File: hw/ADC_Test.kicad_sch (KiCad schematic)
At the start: 63 parts, among them J1 SMA in (perfboard), J2 9V IN, J3 PMOD (ZedBoard), U1 OPA2365, U2 OPA2365, U3 THS4531, U4 ADS7057, U5 AMS1117-3.3, U6 LM393, U7 AMS1117-5.0

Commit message: Add MON output, nWAKE DNP cap, ceramic-stable AVDD LDO, M3 holes
- J4 SMA MON: LPF_OUT through 51R (Basic C23197)
- C31 0603 DNP on nWAKE near J3
- AVDD: XC6206P332 (Basic, ceramic-stable) replaces AMS1117-3.3
- 5 V AMS1117: 22 uF tantalum output per datasheet
- H1/H2 M3 holes, CH silkscreen field, PMOD legend on the back
- README: uses, regulator decision, MON/DNP

Co-Authored-By: Claude Opus 5.5 <noreply@anthropic.com>
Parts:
- removed C24: 22uF 25V, Capacitor_SMD:C_0805_2012Metric, symbol Device:C
- removed U5: AMS1117-3.3, Package_TO_SOT_SMD:SOT-223-3_TabPin2, symbol Auselia:AMS1117-3.3
- added C29: 22uF 10V tantalum, Capacitor_Tantalum_SMD:CP_EIA-3216-18_Kemet-A, symbol Device:C_Polarized
- added C30: 1uF, Capacitor_SMD:C_0603_1608Metric, symbol Device:C
- added C31: DNP, Capacitor_SMD:C_0603_1608Metric, symbol Device:C
- added H1, H2: M3, MountingHole:MountingHole_3.2mm_M3, symbol Mechanical:MountingHole
- added J4: SMA MON (hand-solder), Connector_Coaxial:SMA_Amphenol_132134_Vertical, symbol Connector:Conn_Coaxial
- added R25: 51R, Resistor_SMD:R_0603_1608Metric, symbol Device:R
- added U5: XC6206P332MR-G, Package_TO_SOT_SMD:SOT-23, symbol Auselia:XC6206P332
- C21: value 22uF 25V -> 1uF; footprint Capacitor_SMD:C_0805_2012Metric -> Capacitor_SMD:C_0603_1608Metric; LCSC C45783 -> C15849
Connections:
- net +5V: now also C29.1, C30.1, U5.3 (VIN)
- net AVDD: now also U5.2 (VOUT)
- net GND: now also C29.2, C30.2, C31.2, J4.2 (Ext), U5.1 (VSS)
- net LPF_OUT: now also R25.1
- net WAKE_N: now also C31.1
- new net MON: J4.1 (In), R25.2
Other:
- note added: "AVDD = XC6206P332 from 5 V (also the ADC reference). Ceramic-stable LDO; C18 4.7 uF + C22 100 nF sit at the ADS7057 AVDD pin."
- note added: "C31: optional filter on nWAKE, not fitted. No hysteresis: the outputs are wired together."
- note added: "MON: LPF_OUT through 51R to an SMA for the scope (same signal the ADC samples)."
- note added: "Power: 9 V battery -> SS14 -> AMS1117-5.0 (+5V). AMS1117 needs a 22 uF solid tantalum output capacitor for stability (datasheet)."
- note removed: "AVDD = AMS1117-3.3 from 5 V (also the ADC reference)"
- note removed: "Power: 9 V battery -> SS14 -> AMS1117-5.0 (+5V for op-amps, driver, comparator, AVDD regulator)."

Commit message: Put through-hole parts back in the JLC assembly, apply JLC rotation offsets
- BOM/CPL now include J1-J4 and RV1 (C496549, C492401, C60565, C34845)
- CPL rotations: SOIC +270, SOT-23 -90, SOT-223 +180, tantalum +180
- cost.py reads the BOM and compares JLC-soldered vs self-soldered THT
- finish.py: removes dangling GND stubs, solid GND connection for
  starved thermal pads, joint counts exported by fab.sh
- README: cost table for 2/3/5 boards, through-hole section

Co-Authored-By: Claude Sonnet 5.5 <noreply@anthropic.com>
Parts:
- J2: LCSC (none) -> C492401
- J3: LCSC (none) -> C60565
- J4: value SMA MON (hand-solder) -> SMA MON
- RV1: value 20k trim (hand-solder) -> 20k trim

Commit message: Silkscreen labels and logo, SMA 3D model, ngspice check
- front labels: SENSOR IN, SCOPE OUT, WAKE LEVEL, +9V/GND, CH box
- Auselia mark and name on the front, title on the back
- SMA footprint: 132134-11 (same pads, KiCad ships its 3D model)
- sim/adc_chain.py: DC, AC, noise and comparator window check
- README: silkscreen legend and simulation results

Co-Authored-By: Claude Sonnet 5.5 <noreply@anthropic.com>
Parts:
- J1, J4: footprint Connector_Coaxial:SMA_Amphenol_132134_Vertical -> Connector_Coaxial:SMA_Amphenol_132134-11_Vertical

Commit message: Sensor head board with bias-T (HEAD IN), two separate boards, manual v0.2
- ADC_Head: perfboard charge amp (OPA365, 47 pF, 1M) on 10 x 22 mm, powered through the coax
- ADC_Test: 64 x 32 mm, new HEAD IN SMA with bias-T (L2, R26, C32, C33, R27), SENSOR IN kept
- build scripts take BOARD=head, two sets of fab files, cost model for two orders
- sim/head_bias_t.py (OPA365 model), sim/ths4531_stability_estimate.py
- manual v0.2: board figures regenerated, new section 9 (steps 55 to 60), top view page

Co-Authored-By: Claude Sonnet 5.5 <noreply@anthropic.com>
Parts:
- added C32: 10uF, Capacitor_SMD:C_0603_1608Metric, symbol Device:C
- added C33: 100nF, Capacitor_SMD:C_0603_1608Metric, symbol Device:C
- added C34: 47pF C0G, Capacitor_SMD:C_0402_1005Metric, symbol Device:C
- added C35, C37: 10uF, Capacitor_SMD:C_0402_1005Metric, symbol Device:C
- added C36, C38: 100nF, Capacitor_SMD:C_0402_1005Metric, symbol Device:C
- added J5: SMA HEAD IN, Connector_Coaxial:SMA_Amphenol_132134-11_Vertical, symbol Connector:Conn_Coaxial
- added J6: SMA HEAD OUT, Connector_Coaxial:SMA_Amphenol_132134-11_Vertical, symbol Connector:Conn_Coaxial
- added L1, L2: 470uH, Inductor_SMD:L_1210_3225Metric, symbol Device:L
- added R26: 47R, Resistor_SMD:R_0603_1608Metric, symbol Device:R
- added R27: 1M, Resistor_SMD:R_0603_1608Metric, symbol Device:R
- added R28: 1M, Resistor_SMD:R_0402_1005Metric, symbol Device:R
- added R29, R30: 10k, Resistor_SMD:R_0402_1005Metric, symbol Device:R
- added R31: 49.9R, Resistor_SMD:R_0402_1005Metric, symbol Device:R
- added TP1: PIEZO +, TestPoint:TestPoint_THTPad_D2.0mm_Drill1.0mm, symbol Connector:TestPoint
- added TP2: PIEZO -, TestPoint:TestPoint_THTPad_D2.0mm_Drill1.0mm, symbol Connector:TestPoint
- added U8: OPA365, Package_TO_SOT_SMD:SOT-23-5, symbol Auselia:OPA365
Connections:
- net +5V: now also R26.1
- net GND: now also C32.2, J5.2 (Ext)
- net SIG_IN: now also C33.2, R27.1
- net VMID5: now also R27.2
- new net HAC: C38.1, R31.2
- new net HEAD_LINE: C33.1, J5.1 (In), L2.1
- new net HEAD_PWR: C32.1, L2.2, R26.2
- new net HGND: C35.2, C36.2, C37.2, J6.2 (Ext), R30.2, TP2.1, U8.2 (V-)
- new net HLINE: C38.2, J6.1 (In), L1.1
- new net HOUT: C34.2, R28.2, R31.1, U8.1 (OUT)
- new net HREF: C35.1, R29.2, R30.1, U8.3 (+IN)
- new net HSUM: C34.1, R28.1, TP1.1, U8.4 (-IN)
- new net HV: C36.1, C37.1, L1.2, R29.1, U8.5 (V+)
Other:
- note added: "HEAD IN (J5): bias-T. +5V -> 47R (R26, C32 filter) -> 470 uH (L2) -> coax centre = power for the sensor head. C33 100 nF passes the head's signal to SIG_IN."
- note added: "R27 1M gives SIG_IN a DC level (VMID5). J1 (SMA in) stays as before, for a perfboard or a function generator. Use one input at a time."
- note added: "SENSOR HEAD (own board, same panel). Perfboard charge amp (TRL3): piezo -> summing node HSUM, Rf 1M || Cf 47 pF, Rs 49.9R. Runs from 5 V through the coax (L1), signal returns through C38."
- note added: "Single OPA365 (same die as the OPA2365 on the main board), VREF = 5 V / 2 = 2.5 V (10k/10k + 10 uF), all 0402. Head ground is HGND (a separate board)."

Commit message: One SMA input: the bias-T sits on SENSOR IN (J1), HEAD IN removed; board back to 57 x 32 mm, re-placed and re-routed; manual and README updated
Co-Authored-By: Claude Sonnet 5.5 <noreply@anthropic.com>
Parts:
- removed J5: SMA HEAD IN, Connector_Coaxial:SMA_Amphenol_132134-11_Vertical, symbol Connector:Conn_Coaxial
- J1: value SMA in (perfboard) -> SMA SENSOR IN
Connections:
- net HEAD_LINE: now also J1.1 (In)
- net SIG_IN: no longer J1.1 (In)
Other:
- note added: "R27 1M gives SIG_IN a DC level (VMID5). To feed a function generator or a perfboard instead, remove R26 so the centre pin carries no DC."
- note added: "SENSOR IN (J1) = bias-T for the sensor head. +5V -> 47R (R26, C32 filter) -> 470 uH (L2) -> coax centre. C33 100 nF passes the head's signal to SIG_IN."
- note added: "Sensor head (SMA, bias-T) -> 2nd-order HPF 113 kHz -> gain x4.9 -> 2nd-order LPF 512 kHz -> THS4531 -> 10R/400pF -> ADS7057 -> ZedBoard PMOD."
- note removed: "HEAD IN (J5): bias-T. +5V -> 47R (R26, C32 filter) -> 470 uH (L2) -> coax centre = power for the sensor head. C33 100 nF passes the head's signal to SIG_IN."
- note removed: "Perfboard charge amp (SMA) -> 2nd-order HPF 113 kHz -> gain x4.9 -> 2nd-order LPF 512 kHz -> THS4531 -> 10R/400pF -> ADS7057 -> ZedBoard PMOD."
- note removed: "R27 1M gives SIG_IN a DC level (VMID5). J1 (SMA in) stays as before, for a perfboard or a function generator. Use one input at a time."

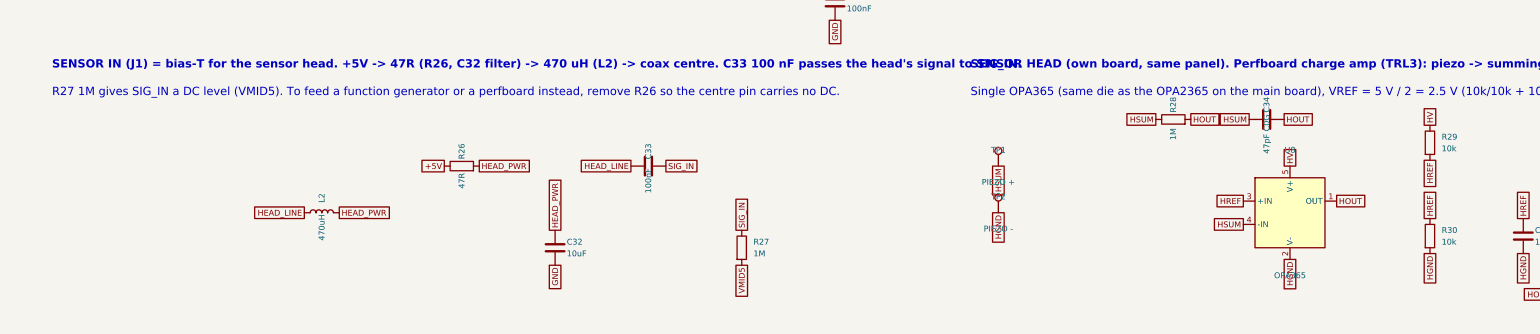
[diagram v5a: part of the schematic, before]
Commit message: Solder jumper JP1 in the head power feed (cut it to use a generator on SENSOR IN); re-routed, files and manual regenerated
Co-Authored-By: Claude Sonnet 5.5 <noreply@anthropic.com>
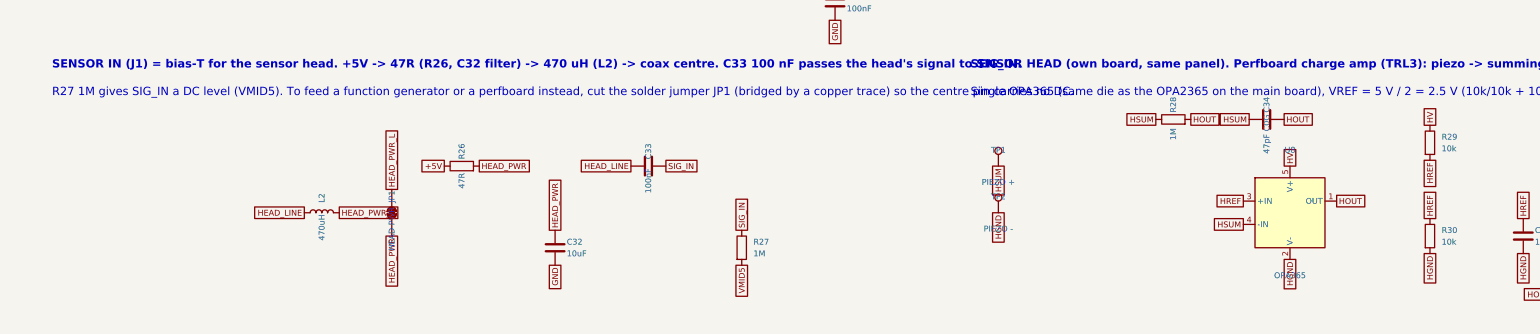
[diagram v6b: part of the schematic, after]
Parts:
- added JP1: HEAD PWR, Jumper:SolderJumper-2_P1.3mm_Bridged_Pad1.0x1.5mm, symbol Jumper:SolderJumper_2_Bridged
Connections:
- net HEAD_PWR: now also JP1.1 (A); no longer L2.2
- new net HEAD_PWR_L: JP1.2 (B), L2.2
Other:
- note added: "R27 1M gives SIG_IN a DC level (VMID5). To feed a function generator or a perfboard instead, cut the solder jumper JP1 (bridged by a copper trace) so the centre pin carries no DC."
- note removed: "R27 1M gives SIG_IN a DC level (VMID5). To feed a function generator or a perfboard instead, remove R26 so the centre pin carries no DC."

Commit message: 5 V input (USB-C and header, SS14 each, ferrite), 18 test points, no 9 V battery, AMS1117 and tantalum removed; chain re-simulated at the 4.6 V rail; manual and README updated
Co-Authored-By: Claude Sonnet 5.5 <noreply@anthropic.com>
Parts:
- removed C29: 22uF 10V tantalum, Capacitor_Tantalum_SMD:CP_EIA-3216-18_Kemet-A, symbol Device:C_Polarized
- removed J2: 9V IN, Connector_PinHeader_2.54mm:PinHeader_1x02_P2.54mm_Vertical, symbol Connector_Generic:Conn_01x02
- removed U7: AMS1117-5.0, Package_TO_SOT_SMD:SOT-223-3_TabPin2, symbol Auselia:AMS1117-5.0
- added D2: SS14, Diode_SMD:D_SMA, symbol Device:D_Schottky
- added FB1: 120R 2A, Inductor_SMD:L_0603_1608Metric, symbol Device:FerriteBead
- added J2: USB-C 5V, Connector_USB:USB_C_Receptacle_HRO_TYPE-C-31-M-12, symbol Connector:USB_C_Receptacle_USB2.0_16P
- added J7: 5V IN, Connector_PinHeader_2.54mm:PinHeader_1x02_P2.54mm_Vertical, symbol Connector_Generic:Conn_01x02
- added R32, R33: 5.1k, Resistor_SMD:R_0603_1608Metric, symbol Device:R
- added TP10: AINM, TestPoint:TestPoint_Pad_D1.5mm, symbol Connector:TestPoint
- added TP11: +5V, TestPoint:TestPoint_Pad_D1.5mm, symbol Connector:TestPoint
- added TP12: AVDD, TestPoint:TestPoint_Pad_D1.5mm, symbol Connector:TestPoint
- added TP13: VMID5, TestPoint:TestPoint_Pad_D1.5mm, symbol Connector:TestPoint
- added TP14: VOCM, TestPoint:TestPoint_Pad_D1.5mm, symbol Connector:TestPoint
- added TP15: +3V3, TestPoint:TestPoint_Pad_D1.5mm, symbol Connector:TestPoint
- added TP16: WAKE_N, TestPoint:TestPoint_Pad_D1.5mm, symbol Connector:TestPoint
- added TP17: VTH_H, TestPoint:TestPoint_Pad_D1.5mm, symbol Connector:TestPoint
- added TP18: VTH_L, TestPoint:TestPoint_Pad_D1.5mm, symbol Connector:TestPoint
- added TP19, TP20: GND, TestPoint:TestPoint_Pad_D1.5mm, symbol Connector:TestPoint
- added TP3: SIG_IN, TestPoint:TestPoint_Pad_D1.5mm, symbol Connector:TestPoint
- added TP4: HPF_OUT, TestPoint:TestPoint_Pad_D1.5mm, symbol Connector:TestPoint
- added TP5: GAIN_OUT, TestPoint:TestPoint_Pad_D1.5mm, symbol Connector:TestPoint
- added TP6: LPF_OUT, TestPoint:TestPoint_Pad_D1.5mm, symbol Connector:TestPoint
- added TP7: DRV_OUTP, TestPoint:TestPoint_Pad_D1.5mm, symbol Connector:TestPoint
- added TP8: DRV_OUTN, TestPoint:TestPoint_Pad_D1.5mm, symbol Connector:TestPoint
- added TP9: AINP, TestPoint:TestPoint_Pad_D1.5mm, symbol Connector:TestPoint
- C23: value 10uF 25V -> 22uF 25V; LCSC C15850 -> C45783
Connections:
- net +3V3: now also TP15.1
- net +5V: now also C23.1, FB1.2, TP11.1
- net AINM: now also TP10.1
- net AINP: now also TP9.1
- net AVDD: now also TP12.1
- net DRV_OUTN: now also TP8.1
- net DRV_OUTP: now also TP7.1
- net GAIN_OUT: now also TP5.1
- net GND: now also J2.A1 (GND), J2.A12 (GND), J2.B1 (GND), J2.B12 (GND), J2.SH (SHIELD), J7.2 (Pin_2), R32.2, R33.2, TP19.1, TP20.1
- net HPF_OUT: now also TP4.1
- net LPF_OUT: now also TP6.1
- net SIG_IN: now also TP3.1
- net VMID5: now also TP13.1
- net VOCM: now also TP14.1
- net VTH_H: now also TP17.1
- net VTH_L: now also TP18.1
- net WAKE_N: now also TP16.1
- net +9VP renamed +5V_IN
- net +5V_IN: now also D2.1 (K), FB1.1; no longer C23.1
- net +9V_IN renamed VBUS
- net VBUS: now also J2.A4 (VBUS), J2.A9 (VBUS), J2.B4 (VBUS), J2.B9 (VBUS)
- new net +5V_EXT: D2.2 (A), J7.1 (Pin_1)
- new net USB_CC1: J2.A5 (CC1), R32.1
- new net USB_CC2: J2.B5 (CC2), R33.1
- no-connect marks 4 -> 10
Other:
- note added: "AFE v0.1 topology rebuilt around JLC Basic parts (100 pF C0G, E12 resistors, AMS1117, LM393). Power: 5 V (USB-C or header) -> SS14 -> ferrite -> +5V, AVDD = XC6206 3.3 V from 5 V. DVDD = PMOD 3.3 V."
- note added: "Power: 5 V from USB-C (J2, CC1/CC2 5.1k request 5 V from any charger) or the 2-pin header J7. SS14 per input = reverse protection and OR. Ferrite FB1 + 22 uF C23 filter the rail."
- note added: "Test points: one after each stage of the signal chain, then the rails, WAKE_N and two grounds for the scope clip."
- note removed: "AFE v0.1 topology rebuilt around JLC Basic parts (100 pF C0G, E12 resistors, AMS1117, LM393). Power: 9 V -> AMS1117-5.0 -> AMS1117-3.3 (AVDD). DVDD = PMOD 3.3 V."
- note removed: "Power: 9 V battery -> SS14 -> AMS1117-5.0 (+5V). AMS1117 needs a 22 uF solid tantalum output capacitor for stability (datasheet)."

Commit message: v3 low-power 3.3 V board: 125 x 21.5 mm narrow layout, PMOD-powered, listener (WAKE_N/BIG_N), routed to 0 unconnected
Manual and README still describe the v2 (5 V, USB-C) board and need regeneration.

Co-Authored-By: Claude Sonnet 5.5 <noreply@anthropic.com>
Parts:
- removed C30: 1uF, Capacitor_SMD:C_0603_1608Metric, symbol Device:C
- removed C31: DNP, Capacitor_SMD:C_0603_1608Metric, symbol Device:C
- removed D1, D2: SS14, Diode_SMD:D_SMA, symbol Device:D_Schottky
- removed FB1: 120R 2A, Inductor_SMD:L_0603_1608Metric, symbol Device:FerriteBead
- removed J2: USB-C 5V, Connector_USB:USB_C_Receptacle_HRO_TYPE-C-31-M-12, symbol Connector:USB_C_Receptacle_USB2.0_16P
- removed R32, R33: 5.1k, Resistor_SMD:R_0603_1608Metric, symbol Device:R
- removed RV1: 20k trim, Potentiometer_THT:Potentiometer_Bourns_3296W_Vertical, symbol Device:R_Potentiometer
- removed U5: XC6206P332MR-G, Package_TO_SOT_SMD:SOT-23, symbol Auselia:XC6206P332
- removed U6: LM393, Package_SO:SOIC-8_3.9x4.9mm_P1.27mm, symbol Auselia:LM393
- added C40, C41: 100pF C0G, Capacitor_SMD:C_0603_1608Metric, symbol Device:C
- added C42: 1uF, Capacitor_SMD:C_0603_1608Metric, symbol Device:C
- added C43, C44, C45: 100nF, Capacitor_SMD:C_0603_1608Metric, symbol Device:C
- added JP2: LISTENER LINK, Jumper:SolderJumper-2_P1.3mm_Bridged_Pad1.0x1.5mm, symbol Jumper:SolderJumper_2_Bridged
- added JP3: CAPTURE LINK, Jumper:SolderJumper-2_P1.3mm_Bridged_Pad1.0x1.5mm, symbol Jumper:SolderJumper_2_Bridged
- added JP4: AVDD LINK, Jumper:SolderJumper-2_P1.3mm_Bridged_Pad1.0x1.5mm, symbol Jumper:SolderJumper_2_Bridged
- added JP5: DVDD LINK, Jumper:SolderJumper-2_P1.3mm_Bridged_Pad1.0x1.5mm, symbol Jumper:SolderJumper_2_Bridged
- added JP6: PMOD 3V3, Jumper:SolderJumper-2_P1.3mm_Bridged_Pad1.0x1.5mm, symbol Jumper:SolderJumper_2_Bridged
- added R34: 10R, Resistor_SMD:R_0603_1608Metric, symbol Device:R
- added R35: 10k, Resistor_SMD:R_0603_1608Metric, symbol Device:R
- added R36: 2.2k, Resistor_SMD:R_0603_1608Metric, symbol Device:R
- added R39, R40: 18k, Resistor_SMD:R_0603_1608Metric, symbol Device:R
- added R41: 33k, Resistor_SMD:R_0603_1608Metric, symbol Device:R
- added R42: 47k, Resistor_SMD:R_0603_1608Metric, symbol Device:R
- added U6, U9: TLV7022, Package_TO_SOT_SMD:SOT-23-8, symbol Auselia:TLV7022
- C21: value 1uF -> 10uF; LCSC C15849 -> C19702
- C23: value 22uF 25V -> 10uF; footprint Capacitor_SMD:C_0805_2012Metric -> Capacitor_SMD:C_0603_1608Metric; LCSC C45783 -> C19702
- J7: value 5V IN -> 3V3 IN
- R21, R23: value 33k -> 1M; LCSC C4216 -> C22935
- R22: value 1.00k -> 33k; LCSC C21190 -> C4216
- R24: value 10k -> 47k; LCSC C25804 -> C25819
- R29, R30: value 10k -> 1M; LCSC C25744 -> C26083
- TP11: value +5V -> +3V3
- TP15: value +3V3 -> LST
- TP17: value VTH_H -> BIG_N
- TP18: value VTH_L -> REFL
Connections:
- net +5V_EXT is gone; now on net +3V3: J7.1 (Pin_1)
- net +3V3: now also C23.1, R26.1, TP11.1, JP2.1 (A), JP3.1 (A), JP5.1 (A), JP6.2 (B), R42.1; no longer C19.1, C20.1, J3.11 (Pin_11), J3.12 (Pin_12), TP15.1, U4.4 (DVDD)
- net AVDD: now also R34.2
- net GND: now also C41.2, C42.2, C43.2, C44.2, C45.2, U6.4 (VEE), U9.4 (VEE)
- net SIG_IN: now also C40.1
- net WAKE_N: now also U6.1 (OUTA), U6.7 (OUTB)
- net BIG_N: now reaches J3.2 (Pin_2)
- net BIG_N: now also TP17.1, R42.2, U9.1 (OUTA), U9.7 (OUTB)
- net +5V renamed +3V3_C
- net +3V3_C: now also JP3.2 (B), JP4.1 (A); no longer C23.1, C28.1, R21.1, R26.1, TP11.1
- net PTOP renamed TH1P
- net TH1P: now also C26.1, R39.1, U6.3 (INA+)
- net VTH_H renamed TH2P
- net TH2P: now also C43.1, U9.3 (INA+); no longer C26.1, TP17.1
- removed net VTH_L: C27.1, R23.1, TP18.1
- new net +3V3_L: C28.1, C45.1, JP2.2 (B), R21.1, U6.8 (VCC), U9.8 (VCC)
- new net +3V3_PMOD: J3.11 (Pin_11), J3.12 (Pin_12), JP6.1 (A)
- new net AVDD_IN: JP4.2 (B), R34.1
- new net DVDD: C19.1, C20.1, JP5.2 (B), U4.4 (DVDD)
- new net LST: C41.1, R36.2, TP15.1, U6.2 (INA-), U6.5 (INB+), U9.2 (INA-), U9.5 (INB+)
- new net LST_A: C40.2, R35.1, R36.1
- new net REFL: C42.1, R35.2, R39.2, R40.1, TP18.1
- new net TH1M: C27.1, R40.2, R41.1, U6.6 (INB-)
- new net TH2M: C44.1, R23.1, R41.2, U9.6 (INB-)
- no-connect marks 10 -> 3
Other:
- note added: "AVDD = +3V3_C through JP4 (current link), R34 10R and C21 10 uF. C18 4.7 uF + C22 100 nF sit at the ADS7057 AVDD pin. DVDD = +3V3 through JP5."
- note added: "Listener (observer, never gates the chain). SIG_IN -> C40 100 pF / R35 10k to REFL (150 kHz high-pass) -> R36 2.2k / C41 100 pF (low-pass) -> LST."
- note added: "Power: +3V3 from the PMOD pins 6 and 12 through JP6 (bridged), or from the 2-pin header J7. Cut JP6 when J7 feeds the board. Current links: JP1 head, JP2 listener, JP3 capture, JP4 AVDD, JP5 DVDD."
- note added: "SENSOR HEAD (own board, same panel). Perfboard charge amp (TRL3): piezo -> summing node HSUM, Rf 1M || Cf 47 pF, Rs 49.9R. Runs from the 3.3 V rail through the coax (L1), signal returns through C38. HQ (default): OPA365 + Cf 47 pF in C34. LP: OPA314 + Cf 100 pF in C34 (0402 C0G C1546)."
- note added: "SENSOR IN (J1) = bias-T for the sensor head. +3V3 -> 47R (R26, C32 filter) -> JP1 -> 470 uH (L2) -> coax centre. C33 100 nF passes the head's signal to SIG_IN."
- note added: "SOT-23-5 for OPA365 or OPA314 (same pinout), VREF = V+/2 (1M/1M + 10 uF, 1.6 uA), all 0402. Head ground is HGND (a separate board)."
- note added: "TLV7022 open-drain comparators. Thresholds from the 1M / 33k / 18k ladder (about +-30 mV and +-84 mV for the 47 pF head, plus 3.6 mV of internal hysteresis). For the 100 pF head use 15k and 6.8k. WAKE_N = small window, BIG_N = large window. Pull-ups R24, R42 to +3V3."
- note added: "ZedBoard PMOD JA..JD (3.3 V). Pin 6/12 = 3.3 V from the ZedBoard = the board's only supply. Pin 10 = WAKE_N, pin 7 = BIG_N (active low)."
- note removed: "AVDD = XC6206P332 from 5 V (also the ADC reference). Ceramic-stable LDO; C18 4.7 uF + C22 100 nF sit at the ADS7057 AVDD pin."
- note removed: "C31: optional filter on nWAKE, not fitted. No hysteresis: the outputs are wired together."
- note removed: "LM393 open-collector outputs are wired together: WAKE_N (PMOD pin 10) is pulled up to 3.3 V and goes LOW when the signal leaves the window."
- note removed: "Power: 5 V from USB-C (J2, CC1/CC2 5.1k request 5 V from any charger) or the 2-pin header J7. SS14 per input = reverse protection and OR. Ferrite FB1 + 22 uF C23 filter the rail."
- note removed: "SENSOR HEAD (own board, same panel). Perfboard charge amp (TRL3): piezo -> summing node HSUM, Rf 1M || Cf 47 pF, Rs 49.9R. Runs from 5 V through the coax (L1), signal returns through C38."
- note removed: "SENSOR IN (J1) = bias-T for the sensor head. +5V -> 47R (R26, C32 filter) -> 470 uH (L2) -> coax centre. C33 100 nF passes the head's signal to SIG_IN."
- note removed: "Single OPA365 (same die as the OPA2365 on the main board), VREF = 5 V / 2 = 2.5 V (10k/10k + 10 uF), all 0402. Head ground is HGND (a separate board)."
- note removed: "Window comparator / wake-up. Half window = 2.5 V x (1k + Rp)/(67k + Rp) = 37 ... 603 mV with the 20k RV1 (about 7 ... 120 mV at the perfboard output)."
- note removed: "ZedBoard PMOD JA..JD (3.3 V). Pin 6/12 = 3.3 V from the ZedBoard -> DVDD. Pin 10 = WAKE_N (active low)."
